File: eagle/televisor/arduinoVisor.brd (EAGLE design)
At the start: 98.1 x 61 mm, 23 parts

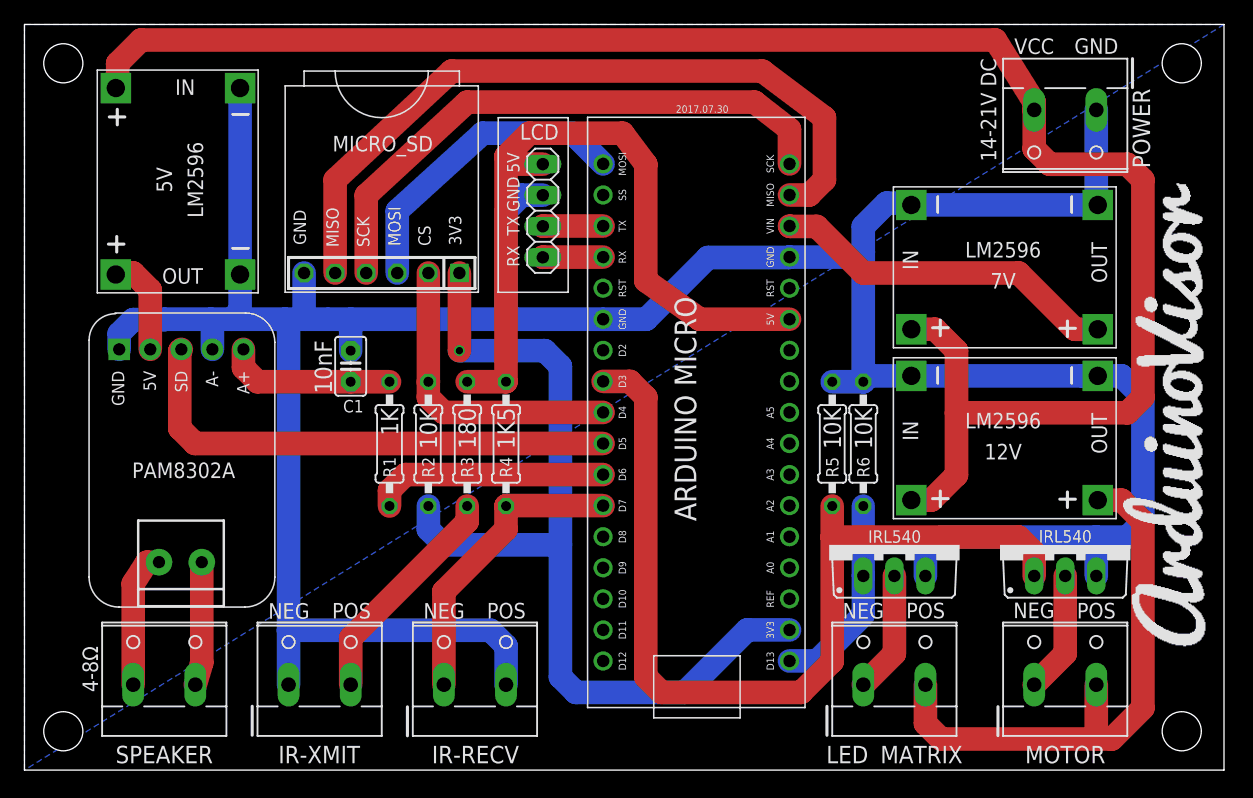
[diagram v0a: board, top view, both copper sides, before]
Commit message: board IR swap pins. ground planes. code uncrustified.
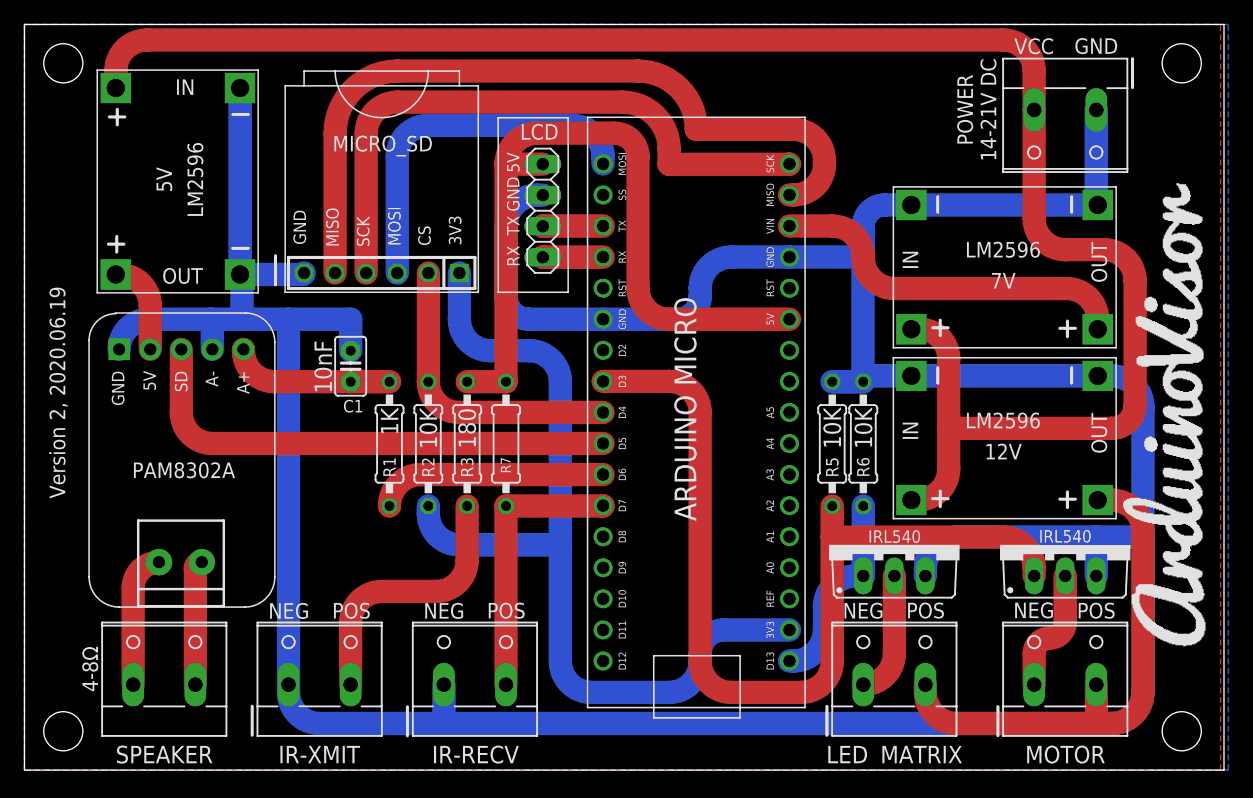
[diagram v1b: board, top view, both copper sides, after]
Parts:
- renumbered R4 to R7
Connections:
- net GND: now also SYNC.1; no longer SYNC.2
- net IR_IN: now also SYNC.2; no longer SYNC.1
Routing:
- net GND: track 257.9 -> 310.3 mm
- net 12VB: track 46.7 -> 41.6 mm
- net MOSI: track 25.4 -> 29.1 mm
- net 3V3: track 75.1 -> 71.8 mm, vias 1 -> 0
- net VCC: track 147.0 -> 144.4 mm
- net IR_OUT: track 18.6 -> 21.2 mm
- net SCK: track 47.5 -> 50.0 mm
- net MOTOR_PWM: track 75.4 -> 73.1 mm
- net IR_IN: track 24.7 -> 22.6 mm
- net SD: track 41.6 -> 40.7 mm
- net 5VB: track 8.30 -> 7.45 mm
- net SPK: track 13.9 -> 13.1 mm
- net LEDS: track 16.5 -> 15.7 mm
- net CS: track 25.0 -> 24.2 mm
- net SOUND: track 19.3 -> 18.5 mm
- added copper zone on layer 1, net GND
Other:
- board text added: "POWER 14-21V DC"
- board text added: "Version 2, 2020.06.19"
- board text removed: "14-21V DC"
- board text removed: "2017.07.30"
- board text removed: "POWER"
